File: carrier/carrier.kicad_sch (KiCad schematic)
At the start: 2 parts, among them J1 DF40TC-30DP-0.4V(51), U1 TC58NVG1S3HBAI6

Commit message: Snapshot Courk-style unrouted NAND interposer
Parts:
- U1: value TC58NVG1S3HBAI6 -> HOME_VFBGA67_INTERFACE; footprint carrier:BGA-67_6.5x8.0mm_Layout8x10_P0.8mm -> carrier:BGA-67_6.5x8.0mm_Layout8x10_P0.8mm_Mirrored_Interposer
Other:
- title: VFBGA67 to DF40 Mezzanine -> Google Home VFBGA67 Chipless Interposer
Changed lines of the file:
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@@
 	(paper "A4")
 	(title_block
-		(title "VFBGA67 to DF40 Mezzanine")
+		(title "Google Home VFBGA67 Chipless Interposer")
 		(date "2026-08-09")
 		(rev "B")
@@
 			)
 		)
-		(property "Value" "TC58NVG1S3HBAI6"
+		(property "Value" "HOME_VFBGA67_INTERFACE"
 			(at 88.5033 49.53 0)
 			(show_name no)
@@
 			)
 		)
-		(property "Footprint" "carrier:BGA-67_6.5x8.0mm_Layout8x10_P0.8mm"
+		(property "Footprint" "carrier:BGA-67_6.5x8.0mm_Layout8x10_P0.8mm_Mirrored_Interposer"
 			(at 63.5 54.61 0)
 			(hide yes)
@@
 			)
 		)
-		(property "Description" ""
+		(property "Description" "Logical pin-map interface for the chipless mirrored VFBGA67 land field soldered to the Google Home motherboard; not a populated NAND."
 			(at 63.5 54.61 0)
 			(show_name no)

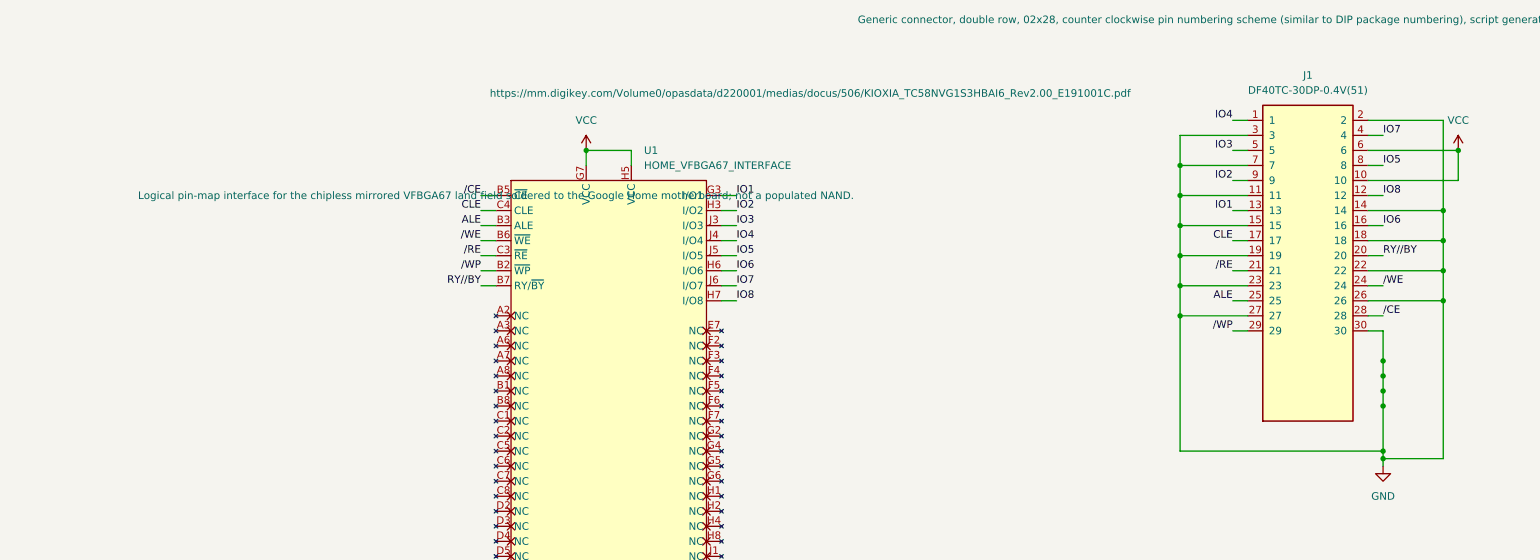
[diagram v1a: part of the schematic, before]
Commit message: Route carrier board
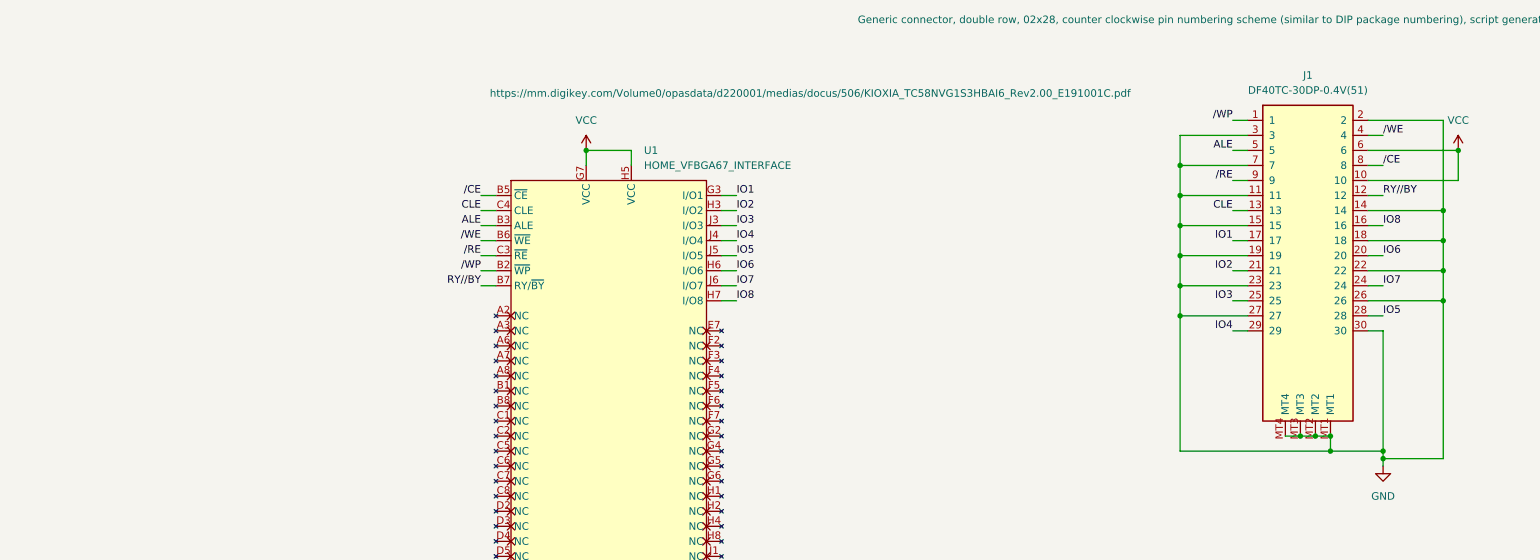
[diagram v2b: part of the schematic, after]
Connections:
- net ALE: now also J1.5; no longer J1.25
- net CLE: now also J1.13; no longer J1.17
- net GND: now also J1.MT1, J1.MT2, J1.MT3, J1.MT4
- net IO1: now also J1.17; no longer J1.13
- net IO2: now also J1.21; no longer J1.9
- net IO3: now also J1.25; no longer J1.5
- net IO4: now also J1.29; no longer J1.1
- net IO5: now also J1.28; no longer J1.8
- net IO6: now also J1.20; no longer J1.16
- net IO7: now also J1.24; no longer J1.4
- net IO8: now also J1.16; no longer J1.12
- net RY//BY: now also J1.12; no longer J1.20
- net /CE: now also J1.8; no longer J1.28
- net /RE: now also J1.9; no longer J1.21
- net /WE: now also J1.4; no longer J1.24
- net /WP: now also J1.1; no longer J1.29
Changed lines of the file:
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@@
+	)
+	(junction
+		(at 204.47 95.25)
+		(diameter 0)
+		(color 0 0 0 0)
 	)
 	(junction
@@
 	)
 	(junction
-		(at 213.36 90.17)
+		(at 204.47 97.79)
 		(diameter 0)
 		(color 0 0 0 0)
@@
 	)
 	(junction
-		(at 213.36 85.09)
-		(diameter 0)
-		(color 0 0 0 0)
-	)
-	(junction
 		(at 179.07 64.77)
 		(diameter 0)
@@
 	)
 	(junction
-		(at 213.36 87.63)
-		(diameter 0)
-		(color 0 0 0 0)
-	)
-	(junction
 		(at 91.44 138.43)
 		(diameter 0)
@@
 	)
 	(junction
+		(at 201.93 95.25)
+		(diameter 0)
+		(color 0 0 0 0)
+	)
+	(junction
 		(at 179.07 59.69)
 		(diameter 0)
@@
 	)
 	(junction
-		(at 213.36 82.55)
-		(diameter 0)
-		(color 0 0 0 0)
-	)
-	(junction
 		(at 83.82 138.43)
 		(diameter 0)
@@
 	)
 	(junction
+		(at 199.39 95.25)
+		(diameter 0)
+		(color 0 0 0 0)
+	)
+	(junction
 		(at 226.06 46.99)
 		(diameter 0)
@@
 	(wire
 		(pts
-			(xy 213.36 87.63) (xy 213.36 90.17)
+			(xy 199.39 95.25) (xy 201.93 95.25)
 		)
 		(stroke
@@
 	(wire
 		(pts
+			(xy 204.47 95.25) (xy 204.47 97.79)
+		)
+		(stroke
+			(width 0)
+			(type default)
+		)
+	)
+	(wire
+		(pts
 			(xy 179.07 74.93) (xy 190.5 74.93)
 		)
@@
 	(wire
 		(pts
-			(xy 179.07 97.79) (xy 213.36 97.79)
+			(xy 179.07 97.79) (xy 204.47 97.79)
 		)
 		(stroke
@@
 	(wire
 		(pts
-			(xy 213.36 82.55) (xy 213.36 85.09)
-		)
-		(stroke
-			(width 0)
-			(type default)
-		)
-	)
-	(wire
-		(pts
 			(xy 210.82 77.47) (xy 213.36 77.47)
 		)
@@
 	(wire
 		(pts
+			(xy 196.85 95.25) (xy 199.39 95.25)
+		)
+		(stroke
+			(width 0)
+			(type default)
+		)
+	)
+	(wire
+		(pts
 			(xy 101.6 67.31) (xy 104.14 67.31)
 		)
@@
 	(wire
 		(pts
-			(xy 213.36 97.79) (xy 213.36 90.17)
+			(xy 213.36 77.47) (xy 213.36 97.79)
+		)
+		(stroke
+			(width 0)
+			(type default)
+		)
+	)
+	(wire
+		(pts
+			(xy 201.93 95.25) (xy 204.47 95.25)
 		)
 		(stroke
@@
 	(wire
 		(pts
+			(xy 204.47 97.79) (xy 213.36 97.79)
+		)
+		(stroke
+			(width 0)
+			(type default)
+		)
+	)
+	(wire
+		(pts
 			(xy 210.82 72.39) (xy 223.52 72.39)
 		)
@@
 	(wire
 		(pts
-			(xy 213.36 85.09) (xy 213.36 87.63)
-		)
-		(stroke
-			(width 0)
-			(type default)
-		)
-	)
-	(wire
-		(pts
-			(xy 213.36 77.47) (xy 213.36 82.55)
-		)
-		(stroke
-			(width 0)
-			(type default)
-		)
-	)
-	(wire
-		(pts
 			(xy 210.82 74.93) (xy 213.36 74.93)
 		)
@@
 	)
 	(label "IO3"
-		(at 187.96 46.99 180)
+		(at 187.96 72.39 180)
 		(effects
 			(font
@@
 	)
 	(label "{slash}WP"
-		(at 187.96 77.47 180)
+		(at 187.96 41.91 180)
 		(effects
 			(font
@@
 	)
 	(label "RY{slash}{slash}BY"
-		(at 213.36 64.77 0)
+		(at 213.36 54.61 0)
 		(effects
 			(font
@@
 	)
 	(label "{slash}CE"
-		(at 213.36 74.93 0)
+		(at 213.36 49.53 0)
 		(effects
 			(font
@@
 	)
 	(label "{slash}RE"
-		(at 187.96 67.31 180)
+		(at 187.96 52.07 180)
 		(effects
 			(font
@@
 	)
 	(label "IO1"
-		(at 187.96 57.15 180)
+		(at 187.96 62.23 180)
 		(effects
 			(font
@@
 	)
 	(label "IO8"
-		(at 213.36 54.61 0)
+		(at 213.36 59.69 0)
 		(effects
 			(font
@@
 	)
 	(label "IO7"
-		(at 213.36 44.45 0)
+		(at 213.36 69.85 0)
 		(effects
 			(font
@@
 	)
 	(label "IO5"
-		(at 213.36 49.53 0)
+		(at 213.36 74.93 0)
 		(effects
 			(font
@@
 	)
 	(label "{slash}WE"
-		(at 213.36 69.85 0)
+		(at 213.36 44.45 0)
 		(effects
 			(font
@@
 	)
 	(label "ALE"
-		(at 187.96 72.39 180)
+		(at 187.96 46.99 180)
 		(effects
 			(font
@@
 	)
 	(label "IO2"
-		(at 187.96 52.07 180)
+		(at 187.96 67.31 180)
 		(effects
 			(font
@@
 	)
 	(label "CLE"
-		(at 187.96 62.23 180)
+		(at 187.96 57.15 180)
 		(effects
 			(font
@@
 	)
 	(label "IO4"
-		(at 187.96 41.91 180)
+		(at 187.96 77.47 180)
 		(effects
 			(font
@@
 	)
 	(label "IO6"
-		(at 213.36 59.69 0)
+		(at 213.36 64.77 0)
 		(effects
 			(font
@@
 		(pin "30"
 		)
+		(pin "MT4"
+		)
+		(pin "MT3"
+		)
+		(pin "MT1"
+		)
+		(pin "MT2"
+		)
 		(instances
 			(project "carrier"
@@
 			)
 		)
-		(property "Description" "Logical pin-map interface for the chipless mirrored VFBGA67 land field soldered to the Google Home motherboard; not a populated NAND."
+		(property "Description" ""
 			(at 63.5 54.61 0)
 			(show_name no)
